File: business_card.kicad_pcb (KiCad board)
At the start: 2 copper layers, 88.9 x 50.8 mm, 14 parts, among them Q1 2N3904, SW1 DS01-254-S-01BE, U1 TLC555IP

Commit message: Set KiCad Board Setup
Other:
- rule pad_to_mask_clearance: 0.1 -> 0.08
- rule solder_mask_min_width: 0.2 -> 0.125
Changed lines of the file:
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@@
 			(dielectric_constraints no)
 		)
-		(pad_to_mask_clearance 0.1)
-		(solder_mask_min_width 0.2)
+		(pad_to_mask_clearance 0.08)
+		(solder_mask_min_width 0.125)
 		(allow_soldermask_bridges_in_footprints no)
 		(pcbplotparams

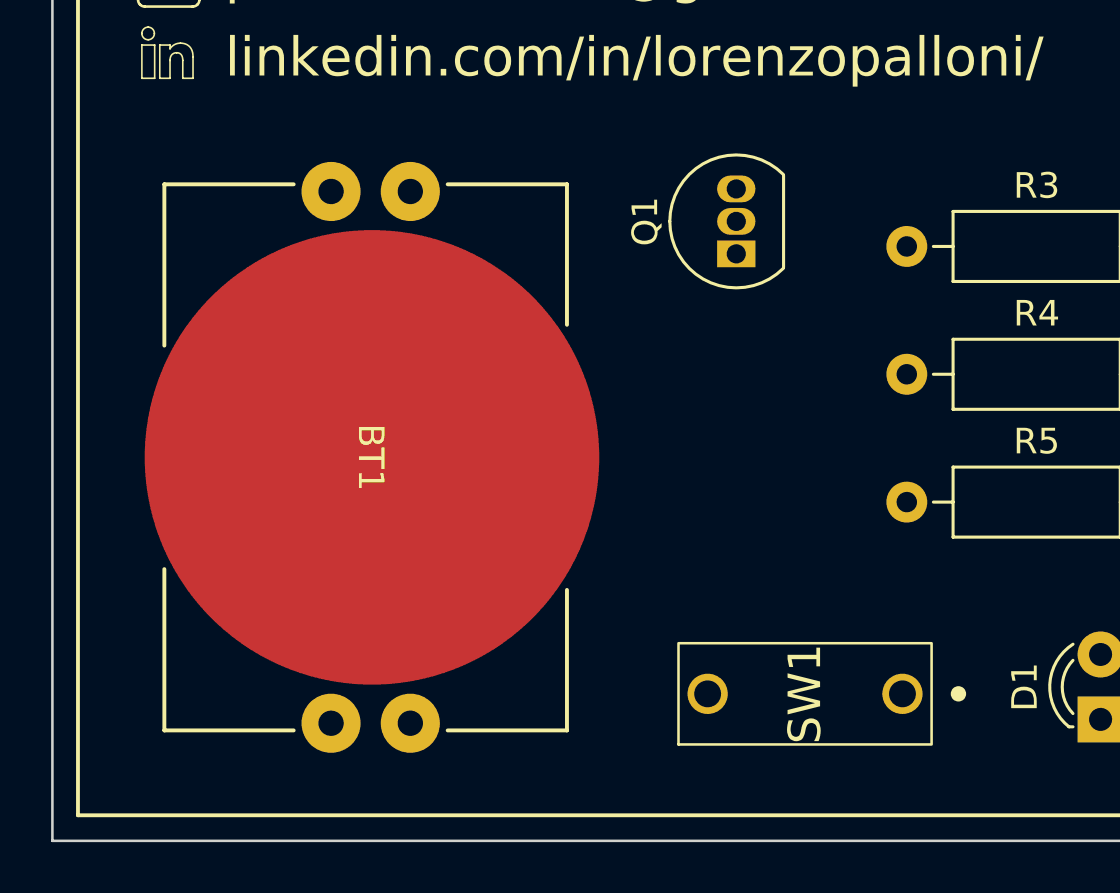
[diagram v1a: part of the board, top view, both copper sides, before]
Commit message: Add battery holder footprint
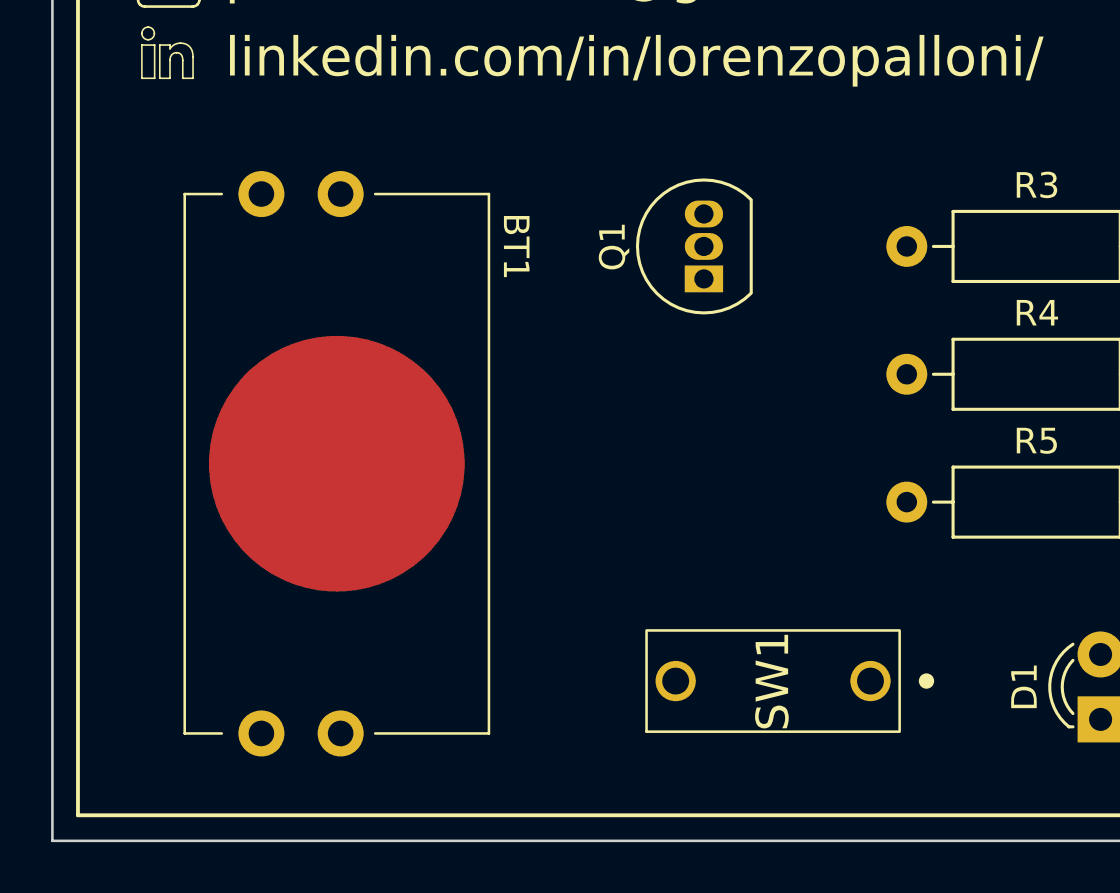
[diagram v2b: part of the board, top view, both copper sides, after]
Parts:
- moved Q1 1.60 mm to (133.5, 107.8)
- moved BT1 1.35 mm to (119.1, 115.0)
- moved SW1 1.35 mm to (136.2, 123.5)
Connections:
- BT1 pad 1: Net-(BT1-+) -> +3V0
- BT1 pad 2: GND -> +3V0
- BT1 pad 3: (no net) -> +3V0
- BT1 pad 4: (no net) -> +3V0
- BT1 pad 5: (no net) -> GND
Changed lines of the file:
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@@
 	(footprint "Package_TO_SOT_THT:TO-92_Inline"
 		(layer "F.Cu")
-		(at 134.75 106.79 90)
+		(at 133.485 107.77 90)
 		(descr "TO-92 leads in-line, narrow, oval pads, drill 0.75mm (see NXP sot054_po.pdf)")
 		(tags "to-92 sc-43 sc-43a sot54 PA33 transistor")
@@
 	(footprint "business_card:DS01-254-S-01BE"
 		(layer "F.Cu")
-		(at 137.44 124 90)
+		(at 136.19 123.5 90)
 		(descr "DIP SWITCH")
 		(tags "Switch")
@@
 	(footprint "business_card:BAT-HLD-001-THM"
 		(layer "F.Cu")
-		(at 120.450001 114.75 -90)
-		(tags "BAT-HLD-001-THM ")
+		(at 119.125 115 -90)
 		(property "Reference" "BT1"
-			(at 0 0 -90)
-			(unlocked yes)
-			(layer "F.SilkS")
-			(effects
-				(font
-					(size 1 1)
-					(thickness 0.15)
+			(at -8.5 -7 -90)
+			(unlocked yes)
+			(layer "F.SilkS")
+			(effects
+				(font
+					(size 1 1)
+					(thickness 0.1)
 				)
 			)
 		)
 		(property "Value" "BAT-HLD-001-THM"
-			(at 0 0 -90)
+			(at 0 1 -90)
 			(unlocked yes)
 			(layer "F.Fab")
@@
 		)
 		(property "Footprint" "business_card:BAT-HLD-001-THM"
-			(at 0 -1.549999 -90)
-			(unlocked yes)
-			(layer "F.Fab")
-			(hide yes)
-			(effects
-				(font
-					(size 1.27 1.27)
+			(at 0 0 -90)
+			(unlocked yes)
+			(layer "F.Fab")
+			(hide yes)
+			(effects
+				(font
+					(size 1 1)
 					(thickness 0.15)
 				)
@@
 		)
 		(property "Datasheet" "https://www.mouser.it/datasheet/2/418/9/ENG_CD_C_BAT_HLD_001_THM_pp_A-3247749.pdf"
-			(at -10.399999 -1.549999 -90)
-			(unlocked yes)
-			(layer "F.Fab")
-			(hide yes)
-			(effects
-				(font
-					(size 1.27 1.27)
+			(at 0 0 -90)
+			(unlocked yes)
+			(layer "F.Fab")
+			(hide yes)
+			(effects
+				(font
+					(size 1 1)
 					(thickness 0.15)
 				)
@@
 		)
 		(property "Description" "Single-cell battery"
-			(at -10.399999 -1.549999 -90)
-			(unlocked yes)
-			(layer "F.Fab")
-			(hide yes)
-			(effects
-				(font
-					(size 1.27 1.27)
+			(at 0 0 -90)
+			(unlocked yes)
+			(layer "F.Fab")
+			(hide yes)
+			(effects
+				(font
+					(size 1 1)
 					(thickness 0.15)
 				)
@@
 		(sheetfile "business_card.kicad_sch")
 		(attr through_hole)
-		(fp_circle
-			(center -11.3157 -1.549999)
-			(end -10.9347 -1.549999)
-			(stroke
-				(width 0.508)
-				(type solid)
+		(fp_line
+			(start -10.55 5.95)
+			(end 10.55 5.95)
+			(stroke
+				(width 0.1)
+				(type default)
+			)
+			(layer "F.SilkS")
+		)
+		(fp_line
+			(start -10.55 4.5)
+			(end -10.55 5.95)
+			(stroke
+				(width 0.1)
+				(type default)
+			)
+			(layer "F.SilkS")
+		)
+		(fp_line
+			(start 10.55 4.5)
+			(end 10.55 5.95)
+			(stroke
+				(width 0.1)
+				(type default)
+			)
+			(layer "F.SilkS")
+		)
+		(fp_line
+			(start -10.55 -5.95)
+			(end -10.55 -1.5)
+			(stroke
+				(width 0.1)
+				(type default)
+			)
+			(layer "F.SilkS")
+		)
+		(fp_line
+			(start -10.55 -5.95)
+			(end 10.55 -5.95)
+			(stroke
+				(width 0.1)
+				(type default)
+			)
+			(layer "F.SilkS")
+		)
+		(fp_line
+			(start 10.55 -5.95)
+			(end 10.55 -1.5)
+			(stroke
+				(width 0.1)
+				(type default)
+			)
+			(layer "F.SilkS")
+		)
+		(fp_rect
+			(start -11.75 -6.25)
+			(end 11.75 8.5)
+			(stroke
+				(width 0.05)
+				(type default)
 			)
 			(fill none)
-			(layer "B.SilkS")
-		)
-		(fp_line
-			(start -10.6807 8.071)
-			(end -4.371304 8.071)
-			(stroke
-				(width 0.1524)
-				(type solid)
-			)
-			(layer "F.SilkS")
-		)
-		(fp_line
-			(start 4.371304 8.071)
-			(end 10.6807 8.071)
-			(stroke
-				(width 0.1524)
-				(type solid)
-			)
-			(layer "F.SilkS")
-		)
-		(fp_line
-			(start 10.6807 8.071)
-			(end 10.6807 3.011732)
-			(stroke
-				(width 0.1524)
-				(type solid)
-			)
-			(layer "F.SilkS")
-		)
-		(fp_line
-			(start -10.6807 3.011732)
-			(end -10.6807 8.071)
-			(stroke
-				(width 0.1524)
-				(type solid)
-			)
-			(layer "F.SilkS")
-		)
-		(fp_line
-			(start 10.6807 -3.011731)
-			(end 10.6807 -7.677)
-			(stroke
-				(width 0.1524)
-				(type solid)
-			)
-			(layer "F.SilkS")
-		)
-		(fp_line
-			(start -10.6807 -7.677)
-			(end -10.6807 -3.011731)
-			(stroke
-				(width 0.1524)
-				(type solid)
-			)
-			(layer "F.SilkS")
-		)
-		(fp_line
-			(start -5.185344 -7.677)
-			(end -10.6807 -7.677)
-			(stroke
-				(width 0.1524)
-				(type solid)
-			)
-			(layer "F.SilkS")
-		)
-		(fp_line
-			(start 10.6807 -7.677)
-			(end 5.185345 -7.677)
-			(stroke
-				(width 0.1524)
-				(type solid)
-			)
-			(layer "F.SilkS")
-		)
-		(fp_line
-			(start -11.809699 9.094)
-			(end 11.8097 9.094)
-			(stroke
-				(width 0.1524)
-				(type solid)
-			)
 			(layer "F.CrtYd")
 		)
-		(fp_line
-			(start 11.8097 9.094)
-			(end 11.8097 -9.194)
-			(stroke
-				(width 0.1524)
-				(type solid)
-			)
-			(layer "F.CrtYd")
-		)
-		(fp_line
-			(start -11.809699 -9.194)
-			(end -11.809699 9.094)
-			(stroke
-				(width 0.1524)
-				(type solid)
-			)
-			(layer "F.CrtYd")
-		)
-		(fp_line
-			(start 11.8097 -9.194)
-			(end -11.809699 -9.194)
-			(stroke
-				(width 0.1524)
-				(type solid)
-			)
-			(layer "F.CrtYd")
-		)
-		(fp_line
-			(start -10.5537 7.944)
-			(end 10.5537 7.944)
-			(stroke
-				(width 0.0254)
-				(type solid)
-			)
-			(layer "F.Fab")
-		)
-		(fp_line
-			(start 10.5537 7.944)
-			(end 10.5537 -7.55)
-			(stroke
-				(width 0.0254)
-				(type solid)
-			)
-			(layer "F.Fab")
-		)
-		(fp_line
-			(start -10.5537 -7.55)
-			(end -10.5537 7.944)
-			(stroke
-				(width 0.0254)
-				(type solid)
-			)
-			(layer "F.Fab")
-		)
-		(fp_line
-			(start 10.5537 -7.55)
-			(end -10.5537 -7.55)
-			(stroke
-				(width 0.0254)
-				(type solid)
-			)
-			(layer "F.Fab")
-		)
-		(fp_circle
-			(center -10.399999 -3.454999)
-			(end -10.018999 -3.454999)
-			(stroke
-				(width 0.508)
-				(type solid)
-			)
-			(fill none)
-			(layer "F.Fab")
-		)
 		(fp_text user "${REFERENCE}"
-			(at 0 0 -90)
+			(at 0 2.5 -90)
 			(unlocked yes)
 			(layer "F.Fab")
@@
 		)
 		(pad "1" thru_hole circle
-			(at -10.399999 -1.549999 270)
-			(size 2.3114 2.3114)
-			(drill 0.9906)
-			(layers "*.Cu" "*.Mask")
-			(remove_unused_layers no)
-			(net 10 "Net-(BT1-+)")
+			(at -10.55 -0.15 270)
+			(size 1.8 1.8)
+			(drill 1)
+			(layers "*.Cu" "*.Mask")
+			(remove_unused_layers no)
+			(net 4 "+3V0")
 			(pinfunction "+")
 			(pintype "passive")
 		)
 		(pad "2" thru_hole circle
-			(at -10.399999 1.55 270)
-			(size 2.3114 2.3114)
-			(drill 0.9906)
-			(layers "*.Cu" "*.Mask")
-			(remove_unused_layers no)
-			(net 2 "GND")
+			(at -10.55 2.95 270)
+			(size 1.8 1.8)
+			(drill 1)
+			(layers "*.Cu" "*.Mask")
+			(remove_unused_layers no)
+			(net 4 "+3V0")
 			(pinfunction "-")
 			(pintype "passive")
 		)
 		(pad "3" thru_hole circle
-			(at 10.4 -1.549999 270)
-			(size 2.3114 2.3114)
-			(drill 0.9906)
-			(layers "*.Cu" "*.Mask")
-			(remove_unused_layers no)
+			(at 10.55 -0.15 270)
+			(size 1.8 1.8)
+			(drill 1)
+			(layers "*.Cu" "*.Mask")
+			(remove_unused_layers no)
+			(net 4 "+3V0")
 		)
 		(pad "4" thru_hole circle
-			(at 10.4 1.55 270)
-			(size 2.3114 2.3114)
-			(drill 0.9906)
-			(layers "*.Cu" "*.Mask")
-			(remove_unused_layers no)
+			(at 10.55 2.95 270)
+			(size 1.8 1.8)
+			(drill 1)
+			(layers "*.Cu" "*.Mask")
+			(remove_unused_layers no)
+			(net 4 "+3V0")
 		)
 		(pad "5" smd circle
-			(at 0 -0.049999 270)
-			(size 17.780001 17.780001)
+			(at 0 0 270)
+			(size 10 10)
 			(layers "F.Cu" "F.Paste" "F.Mask")
+			(net 2 "GND")
 		)
 		(model "${KIPRJMOD}/3D-models/BAT-HLD-001-THM.STEP"
 			(offset
-				(xyz 0 0 0)
+				(xyz 0 -1.5 0)
 			)
 			(scale

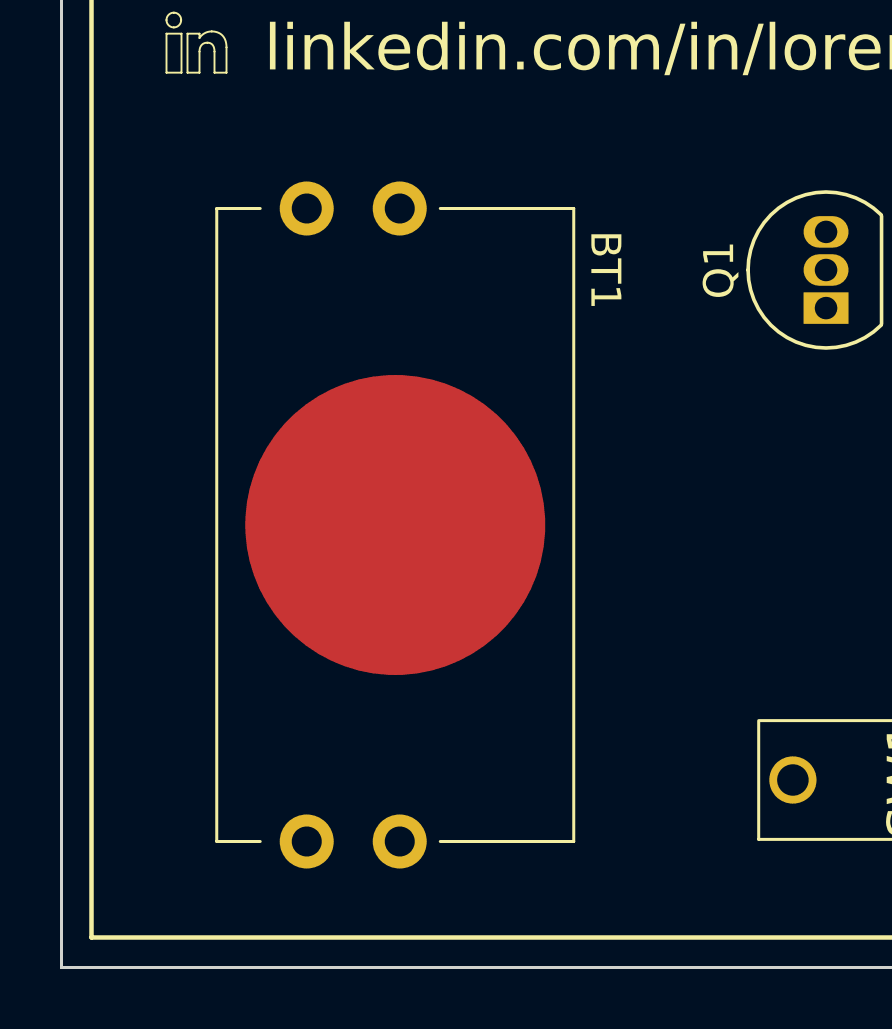
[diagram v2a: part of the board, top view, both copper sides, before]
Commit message: Fix bug on battery holder footprint
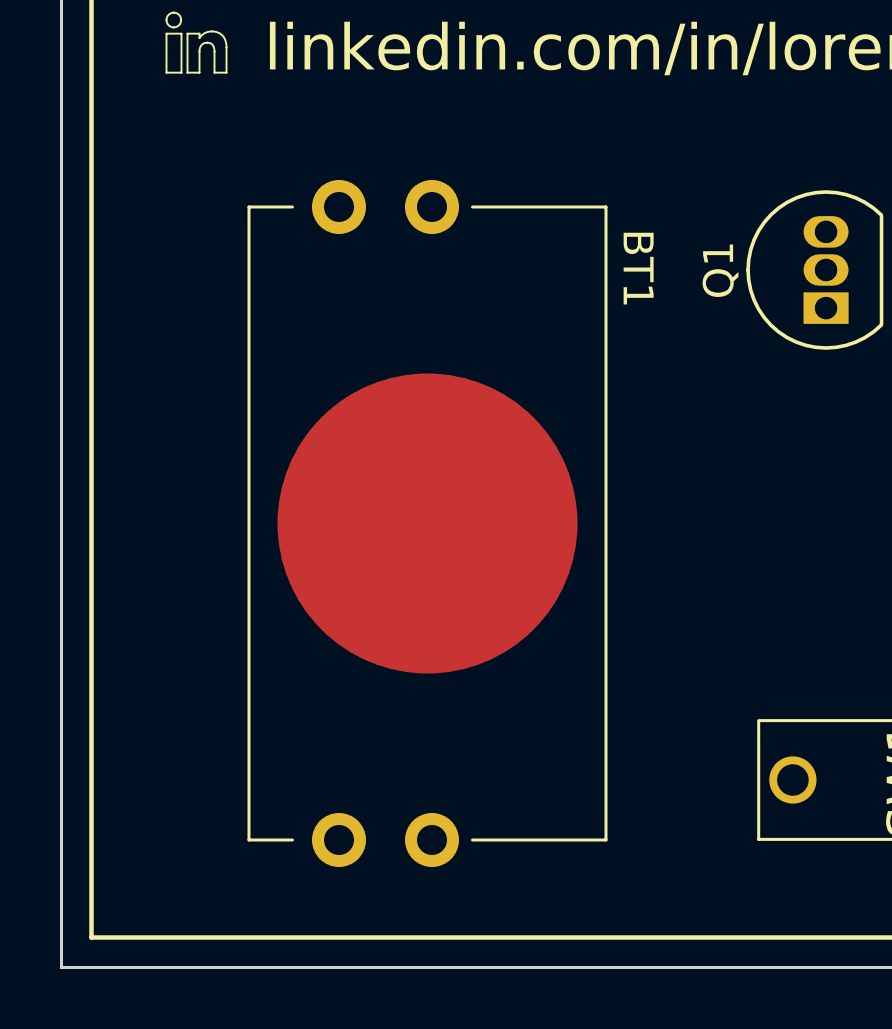
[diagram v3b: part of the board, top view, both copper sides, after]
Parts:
- moved BT1 1.08 mm to (120.2, 115.0)
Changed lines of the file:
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@@
-		)
-	)
-	(footprint "business_card:BAT-HLD-001-THM"
-		(layer "F.Cu")
-		(at 119.125 115 -90)
-		(property "Reference" "BT1"
-			(at -8.5 -7 -90)
-			(unlocked yes)
-			(layer "F.SilkS")
-			(effects
-				(font
-					(size 1 1)
-					(thickness 0.1)
-				)
-			)
-		)
-		(property "Value" "BAT-HLD-001-THM"
-			(at 0 1 -90)
-			(unlocked yes)
-			(layer "F.Fab")
-			(effects
-				(font
-					(size 1 1)
-					(thickness 0.15)
-				)
-			)
-		)
-		(property "Footprint" "business_card:BAT-HLD-001-THM"
-			(at 0 0 -90)
-			(unlocked yes)
-			(layer "F.Fab")
-			(hide yes)
-			(effects
-				(font
-					(size 1 1)
-					(thickness 0.15)
-				)
-			)
-		)
-		(property "Datasheet" "https://www.mouser.it/datasheet/2/418/9/ENG_CD_C_BAT_HLD_001_THM_pp_A-3247749.pdf"
-			(at 0 0 -90)
-			(unlocked yes)
-			(layer "F.Fab")
-			(hide yes)
-			(effects
-				(font
-					(size 1 1)
-					(thickness 0.15)
-				)
-			)
-		)
-		(property "Description" "Single-cell battery"
-			(at 0 0 -90)
-			(unlocked yes)
-			(layer "F.Fab")
-			(hide yes)
-			(effects
-				(font
-					(size 1 1)
-					(thickness 0.15)
-				)
-			)
-		)
-		(sheetname "Root")
-		(sheetfile "business_card.kicad_sch")
-		(attr through_hole)
-		(fp_line
-			(start -10.55 5.95)
-			(end 10.55 5.95)
-			(stroke
-				(width 0.1)
-				(type default)
-			)
-			(layer "F.SilkS")
-		)
-		(fp_line
-			(start -10.55 4.5)
-			(end -10.55 5.95)
-			(stroke
-				(width 0.1)
-				(type default)
-			)
-			(layer "F.SilkS")
-		)
-		(fp_line
-			(start 10.55 4.5)
-			(end 10.55 5.95)
-			(stroke
-				(width 0.1)
-				(type default)
-			)
-			(layer "F.SilkS")
-		)
-		(fp_line
-			(start -10.55 -5.95)
-			(end -10.55 -1.5)
-			(stroke
-				(width 0.1)
-				(type default)
-			)
-			(layer "F.SilkS")
-		)
-		(fp_line
-			(start -10.55 -5.95)
-			(end 10.55 -5.95)
-			(stroke
-				(width 0.1)
-				(type default)
-			)
-			(layer "F.SilkS")
-		)
-		(fp_line
-			(start 10.55 -5.95)
-			(end 10.55 -1.5)
-			(stroke
-				(width 0.1)
-				(type default)
-			)
-			(layer "F.SilkS")
-		)
-		(fp_rect
-			(start -11.75 -6.25)
-			(end 11.75 8.5)
-			(stroke
-				(width 0.05)
-				(type default)
-			)
-			(fill none)
-			(layer "F.CrtYd")
-		)
-		(fp_text user "${REFERENCE}"
-			(at 0 2.5 -90)
-			(unlocked yes)
-			(layer "F.Fab")
-			(effects
-				(font
-					(size 1 1)
-					(thickness 0.15)
-				)
-			)
-		)
-		(pad "1" thru_hole circle
-			(at -10.55 -0.15 270)
-			(size 1.8 1.8)
-			(drill 1)
-			(layers "*.Cu" "*.Mask")
-			(remove_unused_layers no)
-			(net 4 "+3V0")
-			(pinfunction "+")
-			(pintype "passive")
-		)
-		(pad "2" thru_hole circle
-			(at -10.55 2.95 270)
-			(size 1.8 1.8)
-			(drill 1)
-			(layers "*.Cu" "*.Mask")
-			(remove_unused_layers no)
-			(net 4 "+3V0")
-			(pinfunction "-")
-			(pintype "passive")
-		)
-		(pad "3" thru_hole circle
-			(at 10.55 -0.15 270)
-			(size 1.8 1.8)
-			(drill 1)
-			(layers "*.Cu" "*.Mask")
-			(remove_unused_layers no)
-			(net 4 "+3V0")
-		)
-		(pad "4" thru_hole circle
-			(at 10.55 2.95 270)
-			(size 1.8 1.8)
-			(drill 1)
-			(layers "*.Cu" "*.Mask")
-			(remove_unused_layers no)
-			(net 4 "+3V0")
-		)
-		(pad "5" smd circle
-			(at 0 0 270)
-			(size 10 10)
-			(layers "F.Cu" "F.Paste" "F.Mask")
-			(net 2 "GND")
-		)
-		(model "${KIPRJMOD}/3D-models/BAT-HLD-001-THM.STEP"
-			(offset
-				(xyz 0 -1.5 0)
-			)
-			(scale
-				(xyz 1 1 1)
-			)
-			(rotate
-				(xyz -90 0 0)
-			)
 		)
 	)
@@
 			)
 		)
+	)
+	(footprint "business_card:BAT-HLD-001-THM"
+		(layer "F.Cu")
+		(at 120.2 114.95 -90)
+		(property "Reference" "BT1"
+			(at -8.5 -7 -90)
+			(unlocked yes)
+			(layer "F.SilkS")
+			(effects
+				(font
+					(size 1 1)
+					(thickness 0.1)
+				)
+			)
+		)
+		(property "Value" "BAT-HLD-001-THM"
+			(at 0 1 -90)
+			(unlocked yes)
+			(layer "F.Fab")
+			(effects
+				(font
+					(size 1 1)
+					(thickness 0.15)
+				)
+			)
+		)
+		(property "Footprint" "business_card:BAT-HLD-001-THM"
+			(at 0 0 -90)
+			(unlocked yes)
+			(layer "F.Fab")
+			(hide yes)
+			(effects
+				(font
+					(size 1 1)
+					(thickness 0.15)
+				)
+			)
+		)
+		(property "Datasheet" "https://www.mouser.it/datasheet/2/418/9/ENG_CD_C_BAT_HLD_001_THM_pp_A-3247749.pdf"
+			(at 0 0 -90)
+			(unlocked yes)
+			(layer "F.Fab")
+			(hide yes)
+			(effects
+				(font
+					(size 1 1)
+					(thickness 0.15)
+				)
+			)
+		)
+		(property "Description" "Single-cell battery"
+			(at 0 0 -90)
+			(unlocked yes)
+			(layer "F.Fab")
+			(hide yes)
+			(effects
+				(font
+					(size 1 1)
+					(thickness 0.15)
+				)
+			)
+		)
+		(sheetname "Root")
+		(sheetfile "business_card.kicad_sch")
+		(attr through_hole)
+		(fp_line
+			(start -10.55 5.95)
+			(end 10.55 5.95)
+			(stroke
+				(width 0.1)
+				(type default)
+			)
+			(layer "F.SilkS")
+		)
+		(fp_line
+			(start -10.55 4.5)
+			(end -10.55 5.95)
+			(stroke
+				(width 0.1)
+				(type default)
+			)
+			(layer "F.SilkS")
+		)
+		(fp_line
+			(start 10.55 4.5)
+			(end 10.55 5.95)
+			(stroke
+				(width 0.1)
+				(type default)
+			)
+			(layer "F.SilkS")
+		)
+		(fp_line
+			(start -10.55 -5.95)
+			(end -10.55 -1.5)
+			(stroke
+				(width 0.1)
+				(type default)
+			)
+			(layer "F.SilkS")
+		)
+		(fp_line
+			(start -10.55 -5.95)
+			(end 10.55 -5.95)
+			(stroke
+				(width 0.1)
+				(type default)
+			)
+			(layer "F.SilkS")
+		)
+		(fp_line
+			(start 10.55 -5.95)
+			(end 10.55 -1.5)
+			(stroke
+				(width 0.1)
+				(type default)
+			)
+			(layer "F.SilkS")
+		)
+		(fp_rect
+			(start -11.75 -6.25)
+			(end 11.75 8.5)
+			(stroke
+				(width 0.05)
+				(type default)
+			)
+			(fill none)
+			(layer "F.CrtYd")
+		)
+		(fp_text user "${REFERENCE}"
+			(at 0 2.5 -90)
+			(unlocked yes)
+			(layer "F.Fab")
+			(effects
+				(font
+					(size 1 1)
+					(thickness 0.15)
+				)
+			)
+		)
+		(pad "1" thru_hole circle
+			(at -10.55 -0.15 270)
+			(size 1.8 1.8)
+			(drill 1)
+			(layers "*.Cu" "*.Mask")
+			(remove_unused_layers no)
+			(net 4 "+3V0")
+			(pinfunction "+")
+			(pintype "passive")
+		)
+		(pad "2" thru_hole circle
+			(at -10.55 2.95 270)
+			(size 1.8 1.8)
+			(drill 1)
+			(layers "*.Cu" "*.Mask")
+			(remove_unused_layers no)
+			(net 4 "+3V0")
+			(pinfunction "-")
+			(pintype "passive")
+		)
+		(pad "3" thru_hole circle
+			(at 10.55 -0.15 270)
+			(size 1.8 1.8)
+			(drill 1)
+			(layers "*.Cu" "*.Mask")
+			(remove_unused_layers no)
+			(net 4 "+3V0")
+		)
+		(pad "4" thru_hole circle
+			(at 10.55 2.95 270)
+			(size 1.8 1.8)
+			(drill 1)
+			(layers "*.Cu" "*.Mask")
+			(remove_unused_layers no)
+			(net 4 "+3V0")
+		)
+		(pad "5" smd circle
+			(at 0 0 270)
+			(size 10 10)
+			(layers "F.Cu" "F.Paste" "F.Mask")
+			(net 2 "GND")
+		)
+		(model "${KIPRJMOD}/3D-models/BAT-HLD-001-THM.STEP"
+			(offset
+				(xyz 0 -1.5 0)
+			)
+			(scale
+				(xyz 1 1 1)
+			)
+			(rotate
+				(xyz -90 0 0)
+			)
+		)
